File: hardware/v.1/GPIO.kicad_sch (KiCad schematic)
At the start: 12 parts, among them J10 Conn_01x03_Pin, J11 Conn_01x03_Pin, J12 Conn_01x04_Pin, J13 Conn_01x04_Pin, J14 Conn_01x03_Pin, J7 Conn_01x04_Pin, J8 Conn_01x03_Pin, J9 Conn_01x04_Pin, U10 ULC0524P, U11 ULC0524P, U12 ULC0524P, U9 ULC0524P

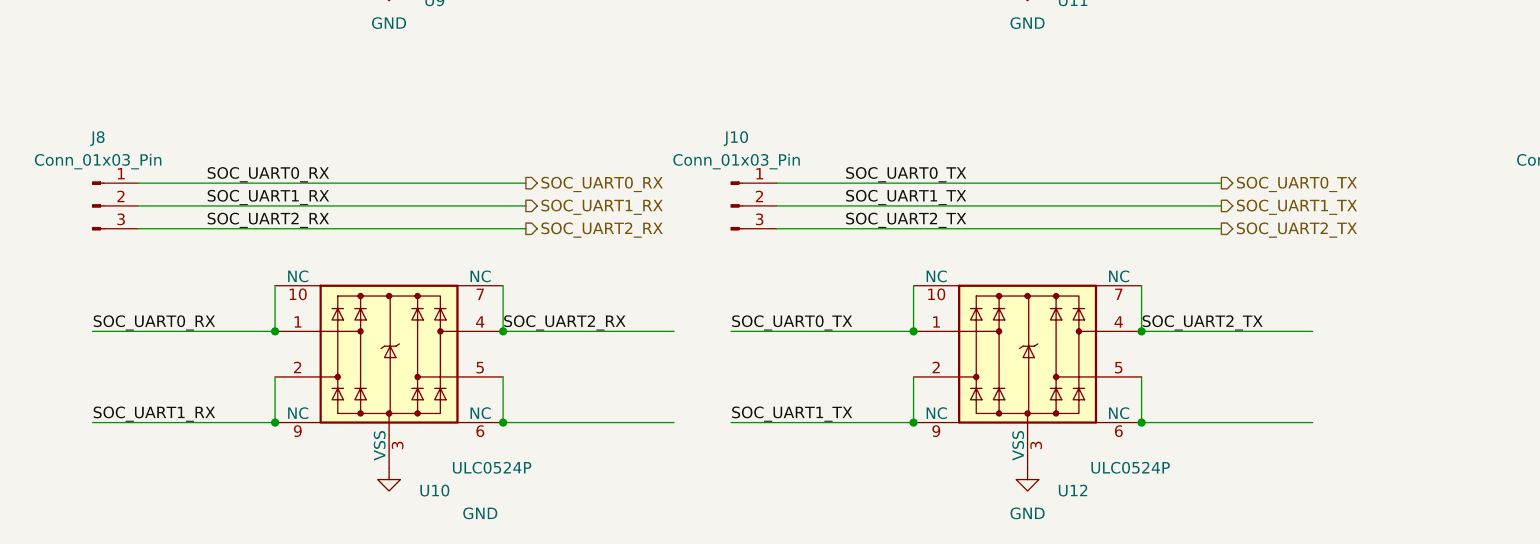
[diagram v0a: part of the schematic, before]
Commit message: fix interrupted ground pour
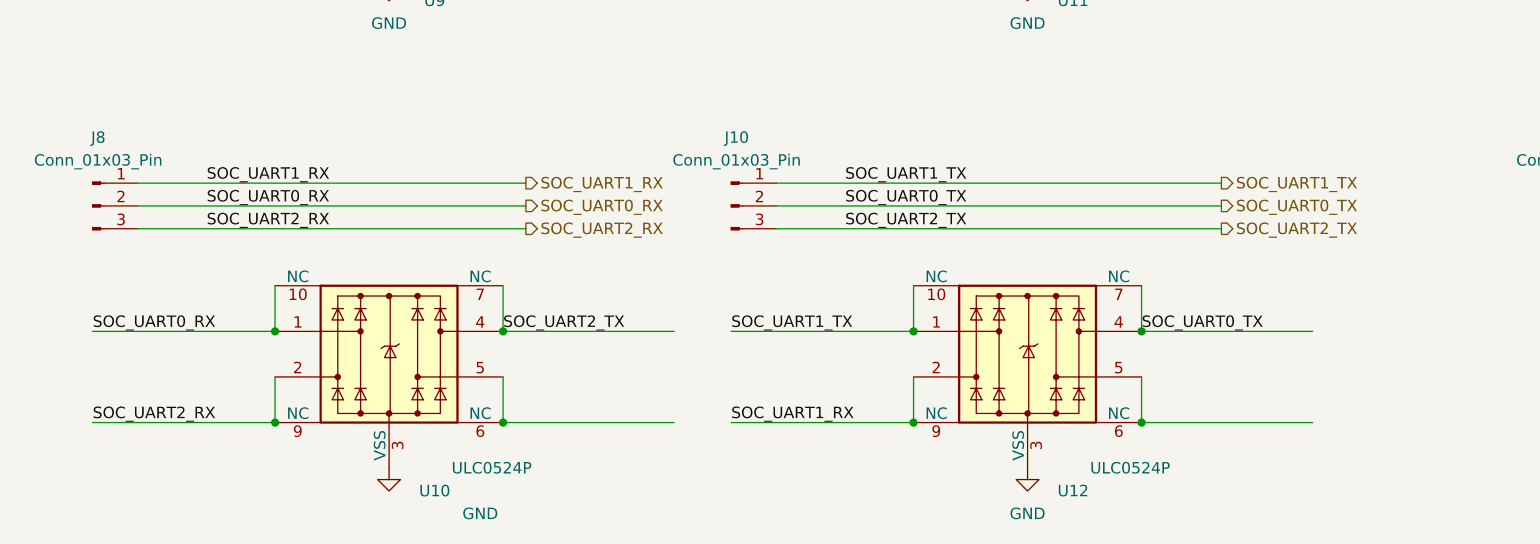
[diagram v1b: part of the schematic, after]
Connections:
- net SOC_UART0_RX: now also J8.2 (Pin_2); no longer J8.1 (Pin_1)
- net SOC_UART0_TX: now also J10.2 (Pin_2), U12.4, U12.7 (NC); no longer J10.1 (Pin_1), U12.1, U12.10 (NC)
- net SOC_UART1_RX: now also J8.1 (Pin_1), U12.2, U12.9 (NC); no longer J8.2 (Pin_2), U10.2, U10.9 (NC)
- net SOC_UART1_TX: now also J10.1 (Pin_1), U12.1, U12.10 (NC); no longer J10.2 (Pin_2), U12.2, U12.9 (NC)
- net SOC_UART2_RX: now also U10.2, U10.9 (NC); no longer U10.4, U10.7 (NC)
- net SOC_UART2_TX: now also U10.4, U10.7 (NC); no longer U12.4, U12.7 (NC)
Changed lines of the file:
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@@
 		)
 	)
-	(label "SOC_UART0_TX"
+	(label "SOC_UART1_TX"
 		(at 302.26 226.06 0)
 		(effects
@@
 		)
 	)
-	(label "SOC_UART1_TX"
+	(label "SOC_UART0_TX"
 		(at 302.26 228.6 0)
 		(effects
@@
 		)
 	)
-	(label "SOC_UART0_TX"
+	(label "SOC_UART1_TX"
 		(at 289.56 242.57 0)
 		(effects
@@
 		)
 	)
+	(label "SOC_UART2_RX"
+		(at 218.44 252.73 0)
+		(effects
+			(font
+				(size 1.27 1.27)
+			)
+			(justify left bottom)
+		)
+	)
 	(label "SOC_UART1_RX"
-		(at 218.44 252.73 0)
-		(effects
-			(font
-				(size 1.27 1.27)
-			)
-			(justify left bottom)
-		)
-	)
-	(label "SOC_UART1_TX"
 		(at 289.56 252.73 0)
 		(effects
@@
 		)
 	)
-	(label "SOC_UART0_RX"
+	(label "SOC_UART1_RX"
 		(at 231.14 226.06 0)
 		(effects
@@
 		)
 	)
-	(label "SOC_UART1_RX"
+	(label "SOC_UART0_RX"
 		(at 231.14 228.6 0)
 		(effects
@@
 		)
 	)
-	(label "SOC_UART2_RX"
+	(label "SOC_UART2_TX"
 		(at 264.16 242.57 0)
 		(effects
@@
 		)
 	)
-	(label "SOC_UART2_TX"
+	(label "SOC_UART0_TX"
 		(at 335.28 242.57 0)
 		(effects
@@
 		)
 	)
-	(hierarchical_label "SOC_UART0_TX"
+	(hierarchical_label "SOC_UART1_TX"
 		(shape output)
 		(at 344.17 226.06 0)
@@
 		)
 	)
-	(hierarchical_label "SOC_UART1_RX"
+	(hierarchical_label "SOC_UART0_RX"
 		(shape output)
 		(at 266.7 228.6 0)
@@
 		)
 	)
-	(hierarchical_label "SOC_UART0_RX"
+	(hierarchical_label "SOC_UART1_RX"
 		(shape output)
 		(at 266.7 226.06 0)
@@
 		)
 	)
-	(hierarchical_label "SOC_UART1_TX"
+	(hierarchical_label "SOC_UART0_TX"
 		(shape output)
 		(at 344.17 228.6 0)

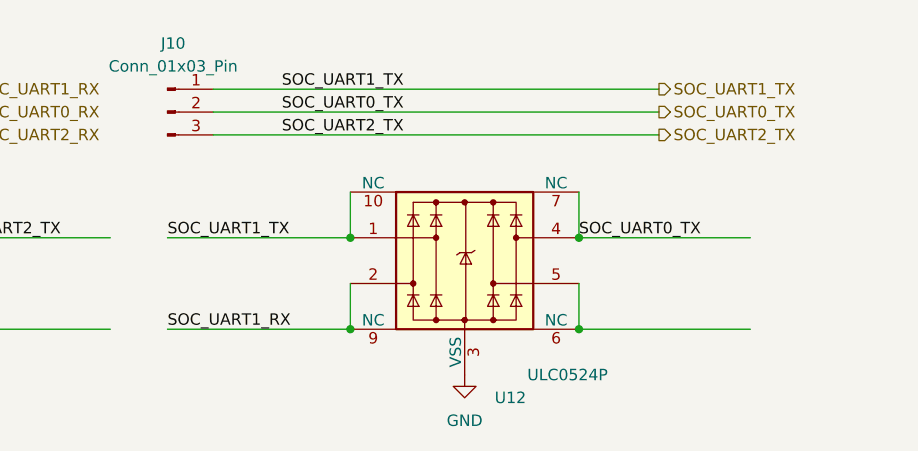
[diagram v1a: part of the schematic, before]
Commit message: fix power supply lines
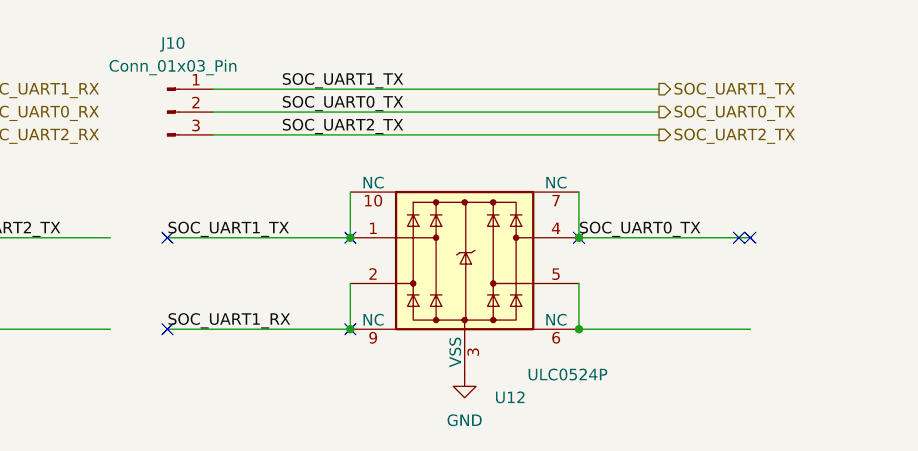
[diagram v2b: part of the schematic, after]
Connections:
- no-connect marks 0 -> 7
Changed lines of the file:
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@@
 		(color 0 0 0 0)
+	)
+	(no_connect
+		(at 309.88 242.57)
+	)
+	(no_connect
+		(at 309.88 252.73)
+	)
+	(no_connect
+		(at 353.06 242.57)
+	)
+	(no_connect
+		(at 289.56 252.73)
+	)
+	(no_connect
+		(at 289.56 242.57)
+	)
+	(no_connect
+		(at 335.28 242.57)
+	)
+	(no_connect
+		(at 354.33 242.57)
 	)
 	(wire
